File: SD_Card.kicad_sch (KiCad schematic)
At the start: 5 parts, among them J8 Micro_SD_Card_Det1

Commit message: Screw Terminal FPs
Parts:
- J8: footprint (none) -> ESP32-S3_Dev_Board:TF-SMD_TF-012; PN (none) -> TF-012-P9
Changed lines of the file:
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@@
       (effects (font (size 1.27 1.27)))
     )
-    (property "Footprint" "" (at 266.065 69.215 0)
+    (property "Footprint" "ESP32-S3_Dev_Board:TF-SMD_TF-012" (at 266.065 69.215 0)
       (effects (font (size 1.27 1.27)) hide)
     )
@@
       (effects (font (size 1.27 1.27)) hide)
     )
+    (property "PN" "TF-012-P9" (at 213.995 86.995 0)
+      (effects (font (size 1.27 1.27)) hide)
+    )

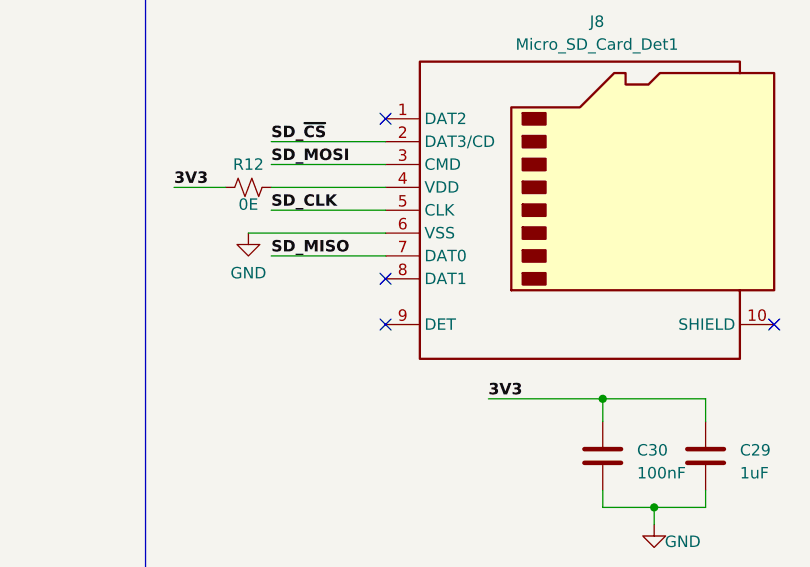
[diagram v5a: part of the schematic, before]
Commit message: Placed ESP32-S3
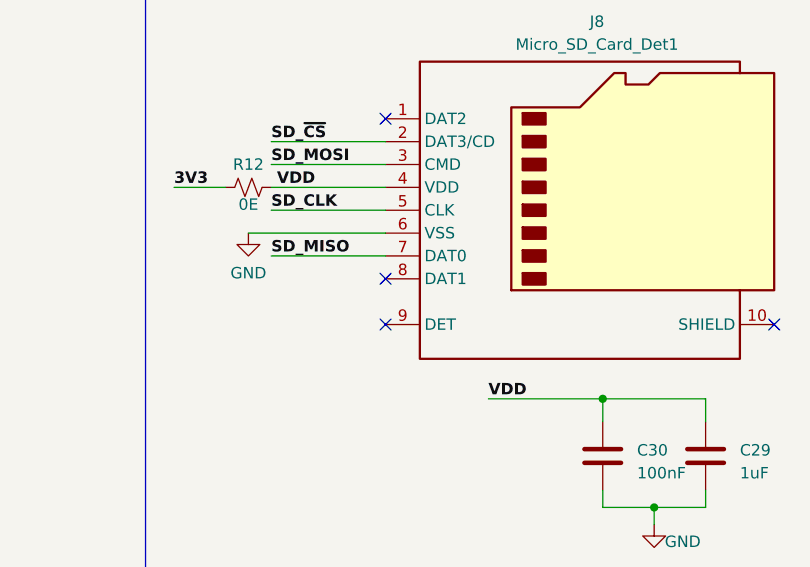
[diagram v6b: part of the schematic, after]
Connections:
- net 3V3: no longer C29.1, C30.1
- net VDD: now reaches J8.4 (VDD), R12.2
- net VDD: now also C29.1, C30.1
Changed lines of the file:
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@@
     (effects (font (size 1.27 1.27) bold (color 204 102 0 1)) (justify left bottom))
+  )
+  (label "VDD" (at 202.565 107.95 0) (fields_autoplaced)
+    (effects (font (size 1.27 1.27) (thickness 0.254) bold (color 194 0 0 1)) (justify left bottom))
   )
   (label "SD_MISO" (at 48.895 178.435 0) (fields_autoplaced)
@@
     (effects (font (size 1.27 1.27) bold (color 204 102 0 1)) (justify left bottom))
   )
-  (label "3V3" (at 202.565 107.95 0) (fields_autoplaced)
-    (effects (font (size 1.27 1.27) bold (color 255 0 0 1)) (justify left bottom))
-  )
   (label "SD_CLK" (at 178.435 86.995 0) (fields_autoplaced)
     (effects (font (size 1.27 1.27) bold (color 204 102 0 1)) (justify left bottom))
   )
+  (label "VDD" (at 179.07 84.455 0) (fields_autoplaced)
+    (effects (font (size 1.27 1.27) (thickness 0.254) bold (color 194 0 0 1)) (justify left bottom))
+  )
   (hierarchical_label "SD_MISO" (shape output) (at 37.465 178.435 180) (fields_autoplaced)

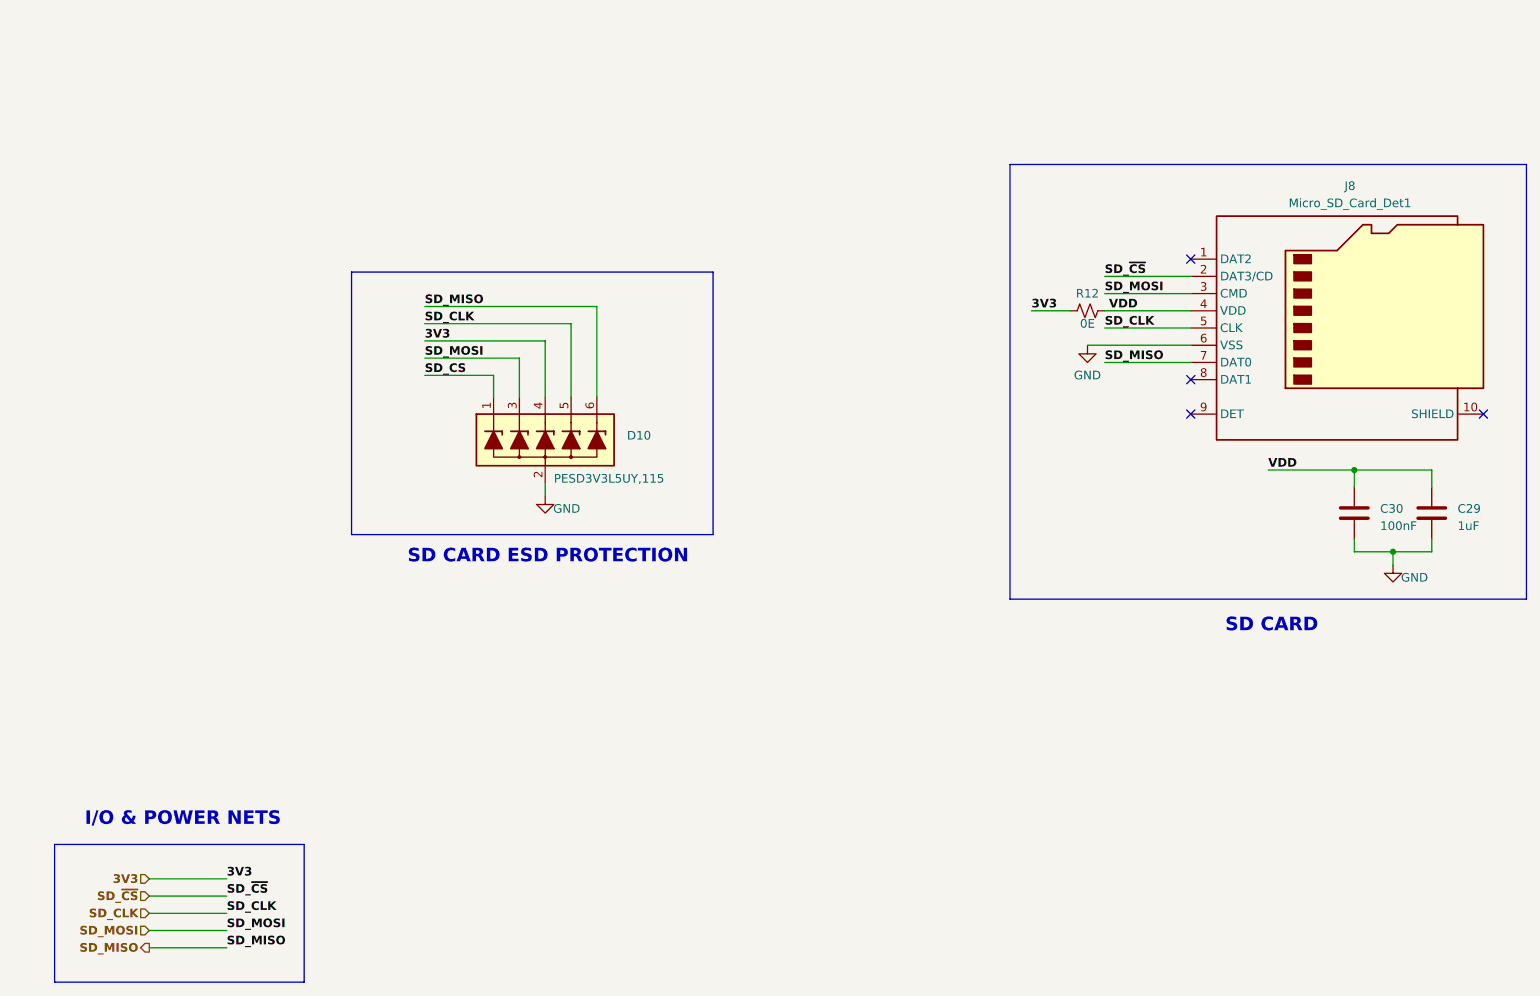
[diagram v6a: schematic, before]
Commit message: Changes CH340 schematic
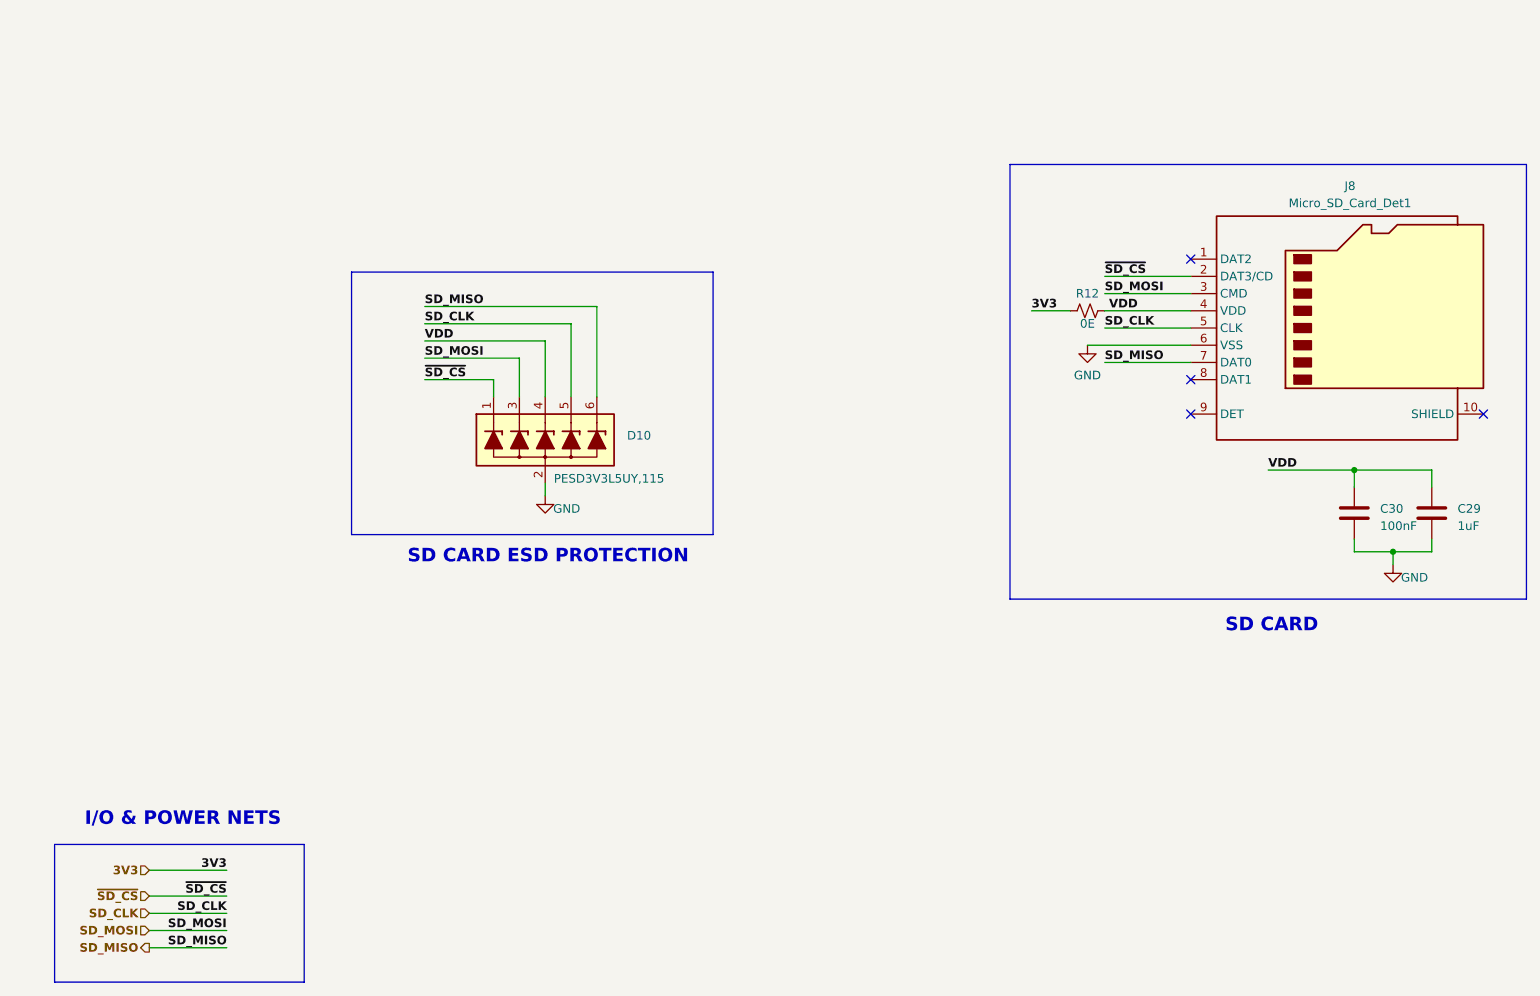
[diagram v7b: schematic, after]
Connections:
- net SD_~{CS} is gone; now on net ~{SD_CS}: J8.2 (DAT3/CD)
- net 3V3: no longer D10.4 (L3)
- net VDD: now also D10.4 (L3)
- net SD_CS renamed ~{SD_CS}
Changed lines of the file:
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@@
     (stroke (width 0) (type default))
   )
-  (wire (pts (xy 48.895 168.275) (xy 37.465 168.275))
+  (wire (pts (xy 48.895 167.005) (xy 37.465 167.005))
     (stroke (width 0.5) (type default) (color 255 0 0 1))
   )
@@
     (stroke (width 0) (type default))
   )
-  (wire (pts (xy 78.105 93.98) (xy 88.265 93.98))
+  (wire (pts (xy 78.105 94.615) (xy 88.265 94.615))
     (stroke (width 0) (type default))
   )
@@
     (stroke (width 0) (type default))
   )
-  (wire (pts (xy 88.265 93.98) (xy 88.265 97.155))
+  (wire (pts (xy 88.265 94.615) (xy 88.265 97.155))
     (stroke (width 0) (type default))
   )
@@
     (effects (font (size 2 2) bold (color 255 0 0 1)) (justify left bottom))
   )
-  (label "SD_~{CS}" (at 178.435 79.375 0) (fields_autoplaced)
-    (effects (font (size 1.27 1.27) bold (color 204 102 0 1)) (justify left bottom))
-  )
-  (label "SD_CS" (at 78.105 93.98 0) (fields_autoplaced)
-    (effects (font (size 1.27 1.27) bold (color 204 102 0 1)) (justify left bottom))
-  )
-  (label "SD_CLK" (at 48.895 173.355 0) (fields_autoplaced)
-    (effects (font (size 1.27 1.27) bold (color 204 102 0 1)) (justify left bottom))
+  (label "SD_CLK" (at 48.895 173.355 180) (fields_autoplaced)
+    (effects (font (size 1.27 1.27) bold (color 204 102 0 1)) (justify right bottom))
   )
   (label "VDD" (at 202.565 107.95 0) (fields_autoplaced)
     (effects (font (size 1.27 1.27) (thickness 0.254) bold (color 194 0 0 1)) (justify left bottom))
   )
-  (label "SD_MISO" (at 48.895 178.435 0) (fields_autoplaced)
-    (effects (font (size 1.27 1.27) bold (color 204 102 0 1)) (justify left bottom))
-  )
-  (label "SD_MOSI" (at 48.895 175.895 0) (fields_autoplaced)
-    (effects (font (size 1.27 1.27) bold (color 204 102 0 1)) (justify left bottom))
-  )
-  (label "3V3" (at 78.105 88.9 0) (fields_autoplaced)
-    (effects (font (size 1.27 1.27) bold (color 255 0 0 1)) (justify left bottom))
+  (label "SD_MISO" (at 48.895 178.435 180) (fields_autoplaced)
+    (effects (font (size 1.27 1.27) bold (color 204 102 0 1)) (justify right bottom))
+  )
+  (label "SD_MOSI" (at 48.895 175.895 180) (fields_autoplaced)
+    (effects (font (size 1.27 1.27) bold (color 204 102 0 1)) (justify right bottom))
   )
   (label "SD_MOSI" (at 178.435 81.915 0) (fields_autoplaced)
@@
     (effects (font (size 1.27 1.27) bold (color 204 102 0 1)) (justify left bottom))
   )
-  (label "3V3" (at 48.895 168.275 0) (fields_autoplaced)
-    (effects (font (size 1.27 1.27) bold (color 255 0 0 1)) (justify left bottom))
+  (label "3V3" (at 48.895 167.005 180) (fields_autoplaced)
+    (effects (font (size 1.27 1.27) bold (color 255 0 0 1)) (justify right bottom))
+  )
+  (label "VDD" (at 78.105 88.9 0) (fields_autoplaced)
+    (effects (font (size 1.27 1.27) (thickness 0.254) bold (color 194 0 0 1)) (justify left bottom))
   )
   (label "SD_MISO" (at 78.105 83.82 0) (fields_autoplaced)
@@
     (effects (font (size 1.27 1.27) bold (color 255 0 0 1)) (justify left bottom))
   )
-  (label "SD_~{CS}" (at 48.895 170.815 0) (fields_autoplaced)
-    (effects (font (size 1.27 1.27) bold (color 204 102 0 1)) (justify left bottom))
+  (label "~{SD_CS}" (at 178.435 79.375 0) (fields_autoplaced)
+    (effects (font (size 1.27 1.27) bold (color 204 102 0 1)) (justify left bottom))
+  )
+  (label "~{SD_CS}" (at 48.895 170.815 180) (fields_autoplaced)
+    (effects (font (size 1.27 1.27) bold (color 204 102 0 1)) (justify right bottom))
   )
   (label "SD_CLK" (at 78.105 86.36 0) (fields_autoplaced)
+    (effects (font (size 1.27 1.27) bold (color 204 102 0 1)) (justify left bottom))
+  )
+  (label "~{SD_CS}" (at 78.105 94.615 0) (fields_autoplaced)
     (effects (font (size 1.27 1.27) bold (color 204 102 0 1)) (justify left bottom))
   )
@@
     (effects (font (size 1.27 1.27) bold (color 204 102 0 1)) (justify right))
   )
-  (hierarchical_label "3V3" (shape input) (at 37.465 168.275 180) (fields_autoplaced)
+  (hierarchical_label "3V3" (shape input) (at 37.465 167.005 180) (fields_autoplaced)
     (effects (font (size 1.27 1.27) bold (color 255 0 0 1)) (justify right))
   )
@@
     (effects (font (size 1.27 1.27) bold (color 204 102 0 1)) (justify right))
   )
-  (hierarchical_label "SD_~{CS}" (shape input) (at 37.465 170.815 180) (fields_autoplaced)
-    (effects (font (size 1.27 1.27) bold (color 204 102 0 1)) (justify right))
-  )
+  (hierarchical_label "~{SD_CS}" (shape input) (at 37.465 170.815 180) (fields_autoplaced)
+    (effects (font (size 1.27 1.27) bold (color 204 102 0 1)) (justify right))
+  )

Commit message: Added HW-Tinkerers logo and supporting graphics
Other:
- company: (none) -> HW-TINKERERS (hw.tinkerers@gmail.com)
- title: (none) -> HARDWARE TINKERERS ESP32-S3 DB
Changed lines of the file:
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@@
 (kicad_sch (version 20230121) (generator eeschema)
   (paper "A4")
+  (title_block
+    (title "HARDWARE TINKERERS ESP32-S3 DB")
+    (rev "1.0.0")
+    (company "HW-TINKERERS (hw.tinkerers@gmail.com)")
+    (comment 1 "Email: bhandarkasrishtikr111@gmail.com")
+    (comment 2 "Author: Srishtik Bhandarkar")
+    (comment 3 "Email: vaibhavkhatri00@gmail.com")
+    (comment 4 "Author: Vaibhav Khatri")
+    (comment 5 "Official HW-Tinkerers email: hw.tinkerers@gmail.com")
+  )
   (junction (at 220.98 120.015) (diameter 0) (color 0 0 0 0)
   )
